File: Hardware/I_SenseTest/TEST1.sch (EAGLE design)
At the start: 18 parts

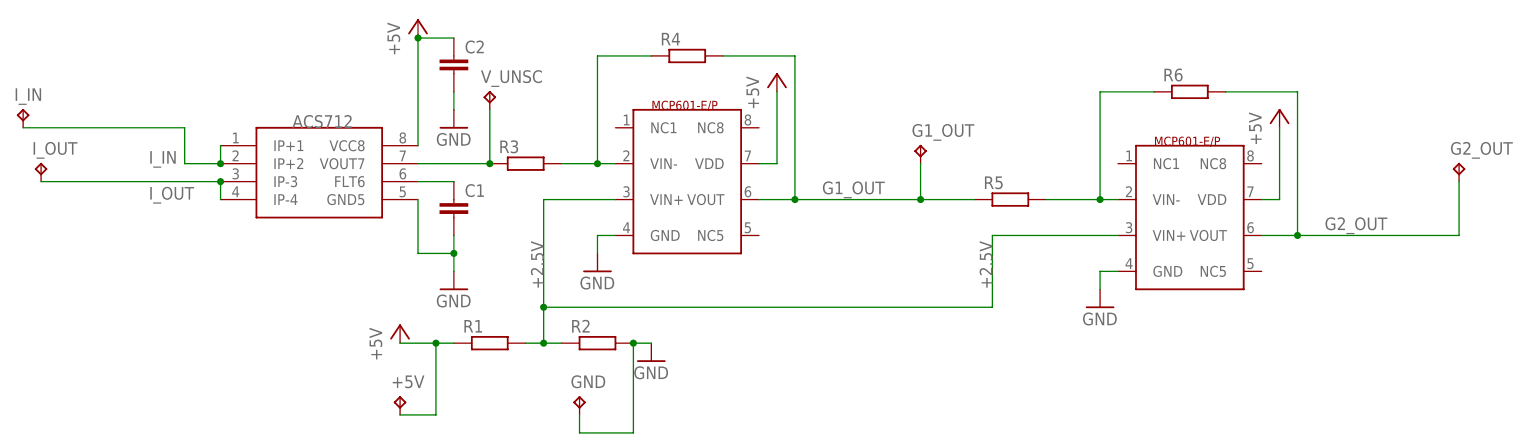
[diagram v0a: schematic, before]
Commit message: Updated the Main Board
Main Board is Fully Done. need to Test the timing circuit before sending
the design for manufacture
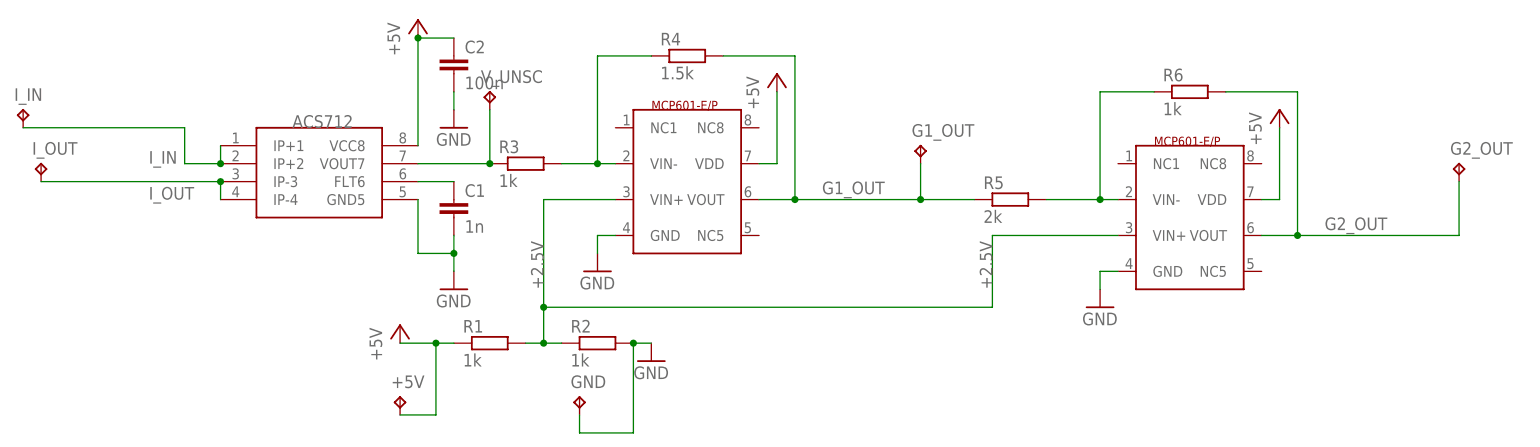
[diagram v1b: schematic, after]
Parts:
- C1: value (none) -> 1n
- C2: value (none) -> 100n
- R1, R2, R3, R6: value (none) -> 1k
- R4: value (none) -> 1.5k
- R5: value (none) -> 2k
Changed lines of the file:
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@@
 <part name="U$1" library="Pauls_parts" deviceset="ACS712" device=""/>
 <part name="U$2" library="Pauls_parts" deviceset="MCP601" device=""/>
-<part name="C1" library="resistor" deviceset="C-EU" device="050-050X075"/>
-<part name="C2" library="resistor" deviceset="C-EU" device="050-050X075"/>
-<part name="R1" library="resistor" deviceset="R-EU_" device="0309/12"/>
-<part name="R2" library="resistor" deviceset="R-EU_" device="0309/12"/>
-<part name="R3" library="resistor" deviceset="R-EU_" device="0309/12"/>
-<part name="R4" library="resistor" deviceset="R-EU_" device="0309/12"/>
+<part name="C1" library="resistor" deviceset="C-EU" device="050-050X075" value="1n"/>
+<part name="C2" library="resistor" deviceset="C-EU" device="050-050X075" value="100n"/>
+<part name="R1" library="resistor" deviceset="R-EU_" device="0309/12" value="1k"/>
+<part name="R2" library="resistor" deviceset="R-EU_" device="0309/12" value="1k"/>
+<part name="R3" library="resistor" deviceset="R-EU_" device="0309/12" value="1k"/>
+<part name="R4" library="resistor" deviceset="R-EU_" device="0309/12" value="1.5k"/>
 <part name="P+1" library="supply1" deviceset="+5V" device=""/>
 <part name="GND1" library="supply1" deviceset="GND" device=""/>
@@
 <part name="GND" library="testpad" deviceset="TP" device="PAD1-17Y"/>
 <part name="U$3" library="Pauls_parts" deviceset="MCP601" device=""/>
-<part name="R5" library="resistor" deviceset="R-EU_" device="0309/12"/>
-<part name="R6" library="resistor" deviceset="R-EU_" device="0309/12"/>
+<part name="R5" library="resistor" deviceset="R-EU_" device="0309/12" value="2k"/>
+<part name="R6" library="resistor" deviceset="R-EU_" device="0309/12" value="1k"/>
 <part name="P+4" library="supply1" deviceset="+5V" device=""/>
 <part name="GND5" library="supply1" deviceset="GND" device=""/>
